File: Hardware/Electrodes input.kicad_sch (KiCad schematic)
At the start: 47 parts, among them J2 Conn_01x26_Pin, U2 TPD4E1B06DRLR

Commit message: DIY_EEG board design changes
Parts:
- removed R1, R10, R11, R12, R13, R14, R15, R16, R2, R3, R4, R5, R6, R7, R8, R9: 220, Resistor_SMD:R_0603_1608Metric, symbol Device:R_US
- removed U2 (x3): TPD4E1B06DRLR, ESD:DRL6_TEX, symbol 2024-02-26_11-45-18:TPD4E1B06DRLR
- added C26: 6.8 uF, Capacitor_SMD:C_0201_0603Metric, symbol Device:C_Small
- added RN1, RN2, RN3, RN4: 4.99 K, Resistor_SMD:R_Array_Convex_4x0402, symbol Device:R_Pack04
- added U3, U4, U5: TPD4E1B06DRLR, tpd4e1b06:DRL6_TEX, symbol 2024-02-26_11-45-18:TPD4E1B06DRLR
- C11, C12, C13, C14, C15, C16, C17, C18, C28, C31, C32, C33, C34, C35, C36, C37, C38, C39: footprint Capacitor_SMD:C_0603_1608Metric_Pad1.08x0.95mm_HandSolder -> Capacitor_SMD:C_0201_0603Metric
- C30: footprint (none) -> Capacitor_SMD:C_0201_0603Metric
- J2: footprint (none) -> Connector_PinHeader_2.54mm:PinHeader_2x13_P2.54mm_Horizontal
- R17: footprint Resistor_SMD:R_0603_1608Metric -> Resistor_SMD:R_0201_0603Metric
- R18, R19, R20, R22: value 220 -> 4.99 K; footprint Resistor_SMD:R_0603_1608Metric -> Resistor_SMD:R_0201_0603Metric
- U2: footprint ESD:DRL6_TEX -> tpd4e1b06:DRL6_TEX
- U6, U9: renamed from U2; footprint ESD:DRL6_TEX -> tpd4e1b06:DRL6_TEX
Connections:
- net AVDD_ED: now also J2.25 (Pin_25), J2.26 (Pin_26); no longer J2.1 (Pin_1), J2.2 (Pin_2)
- net BIAS: now also J2.21 (Pin_21), J2.22 (Pin_22); no longer J2.5 (Pin_5), J2.6 (Pin_6)
- net GNDA: now also C13.1, C17.1, J2.1 (Pin_1), J2.2 (Pin_2), J2.23 (Pin_23), J2.24 (Pin_24), U9.2 (GND), U9.6 (IO4), C26.1, U3.2 (GND), U4.2 (GND), U5.2 (GND); no longer C13.2, C17.2, J2.25 (Pin_25), J2.26 (Pin_26)
- net IN1N: now also C12.2, RN1.2 (R2.1)
- net IN1P: now also C11.2, RN1.1 (R1.1)
- net IN2N: now also C36.2, RN1.4 (R4.1)
- net IN2P: now also C26.2, RN1.3 (R3.1)
- net IN3N: now also C14.2, RN3.2 (R2.1)
- net IN3P: now also C13.2, RN3.1 (R1.1)
- net IN4N: now also C35.2, RN3.4 (R4.1)
- net IN4P: now also C34.2, RN3.3 (R3.1)
- net IN5N: now also C16.2, RN2.2 (R2.1)
- net IN5P: now also C15.2, RN2.1 (R1.1)
- net IN6N: now also C31.2, RN2.4 (R4.1)
- net IN6P: now also C28.2, RN2.3 (R3.1)
- net IN7N: now also C18.2, RN4.2 (R2.1)
- net IN7P: now also C17.2, RN4.1 (R1.1)
- net IN8N: now also C33.2, RN4.4 (R4.1)
- net IN8P: now also C32.2, RN4.3 (R3.1)
- net N1: now also J2.6 (Pin_6), RN1.7 (R2.2); no longer C36.2, J2.21 (Pin_21)
- net N2: now also J2.8 (Pin_8), U2.6 (IO4), RN1.5 (R4.2); no longer C12.2, J2.19 (Pin_19), U2.4 (IO3)
- net N3: now also J2.10 (Pin_10), RN3.7 (R2.2), U3.1 (IO1); no longer C13.1, J2.17 (Pin_17)
- net N4: now also J2.12 (Pin_12), RN3.5 (R4.2), U3.6 (IO4); no longer C35.2, J2.15 (Pin_15)
- net N5: now also J2.14 (Pin_14), RN2.7 (R2.2), U4.1 (IO1); no longer C31.2, J2.13 (Pin_13)
- net N6: now also J2.16 (Pin_16), RN2.5 (R4.2), U4.6 (IO4); no longer C28.2, J2.11 (Pin_11)
- net N7: now also J2.18 (Pin_18), RN4.7 (R2.2), U5.1 (IO1); no longer C17.1, J2.9 (Pin_9)
- net N8: now also J2.20 (Pin_20), RN4.5 (R4.2), U5.6 (IO4); no longer C18.2, J2.7 (Pin_7)
- net P1: now also J2.5 (Pin_5), RN1.8 (R1.2); no longer C11.2, J2.22 (Pin_22)
- net P2: now also J2.7 (Pin_7), U2.4 (IO3), RN1.6 (R3.2); no longer J2.20 (Pin_20), U2.6 (IO4)
- net P3: now also J2.9 (Pin_9), RN3.8 (R1.2), U3.3 (IO2); no longer C34.2, J2.18 (Pin_18)
- net P4: now also J2.11 (Pin_11), RN3.6 (R3.2), U3.4 (IO3); no longer C14.2, J2.16 (Pin_16)
- net P5: now also J2.13 (Pin_13), RN2.8 (R1.2), U4.3 (IO2); no longer C15.2, J2.14 (Pin_14)
- net P6: now also J2.15 (Pin_15), RN2.6 (R3.2), U4.4 (IO3); no longer C16.2, J2.12 (Pin_12)
- net P7: now also J2.17 (Pin_17), RN4.8 (R1.2), U5.3 (IO2); no longer C33.2, J2.10 (Pin_10)
- net P8: now also J2.19 (Pin_19), RN4.6 (R3.2), U5.4 (IO3); no longer C32.2, J2.8 (Pin_8)
- net REF1: now also J2.3 (Pin_3); no longer J2.23 (Pin_23)
- net REF2: now also J2.4 (Pin_4); no longer J2.24 (Pin_24)
- removed net AGND: J2.3 (Pin_3), J2.4 (Pin_4), U9.6 (IO4)
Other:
- moved on the sheet: U2

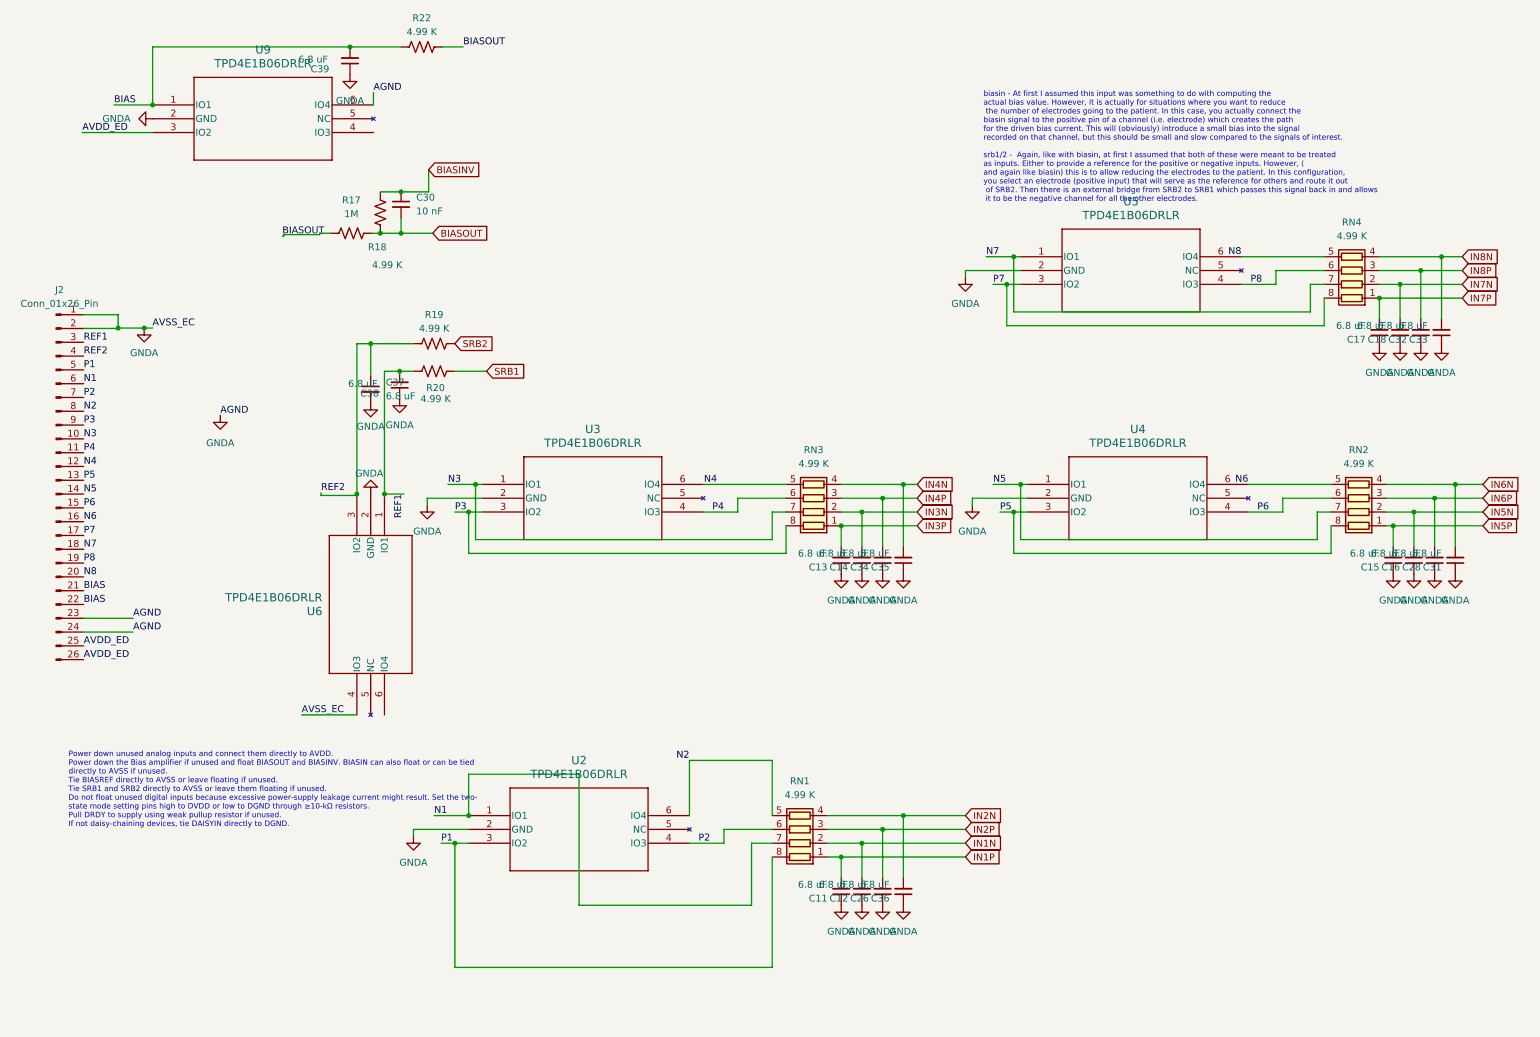
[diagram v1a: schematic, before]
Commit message: redone analog inputs, passive component footprints now match real components, added library for possible 4 element capacitor array
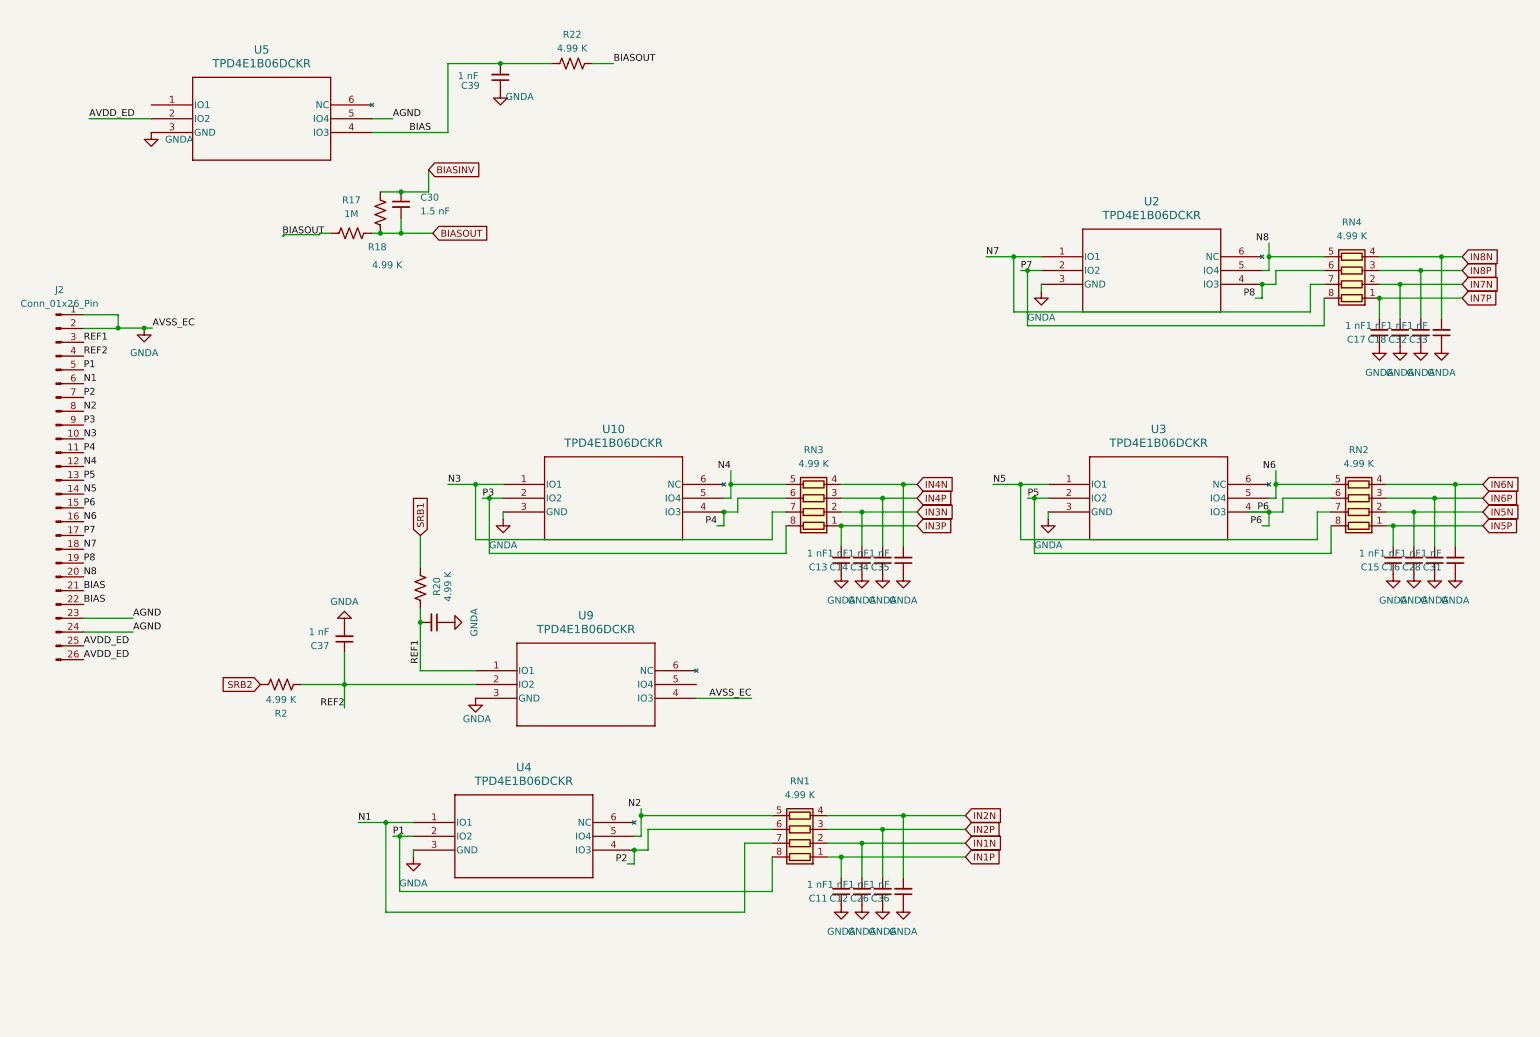
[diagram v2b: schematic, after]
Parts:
- removed R19: 4.99 K, Resistor_SMD:R_0201_0603Metric, symbol Device:R_US
- removed U2, U3, U4, U5, U6, U9: TPD4E1B06DRLR, tpd4e1b06:DRL6_TEX, symbol 2024-02-26_11-45-18:TPD4E1B06DRLR
- added R2: 4.99 K, Resistor_SMD:R_0603_1608Metric, symbol Device:R_US
- added U10, U3, U4, U9: TPD4E1B06DCKR, symbol tpd4e1_esayGND:TPD4E1B06DCKR
- added U2, U5: TPD4E1B06DCKR, TPD4E1B06_R:DCK6_TEX, symbol tpd4e1_esayGND:TPD4E1B06DCKR
- C11, C12, C13, C14, C15, C16, C17, C18, C26, C28, C31, C32, C33, C34, C35, C36, C37, C38, C39: value 6.8 uF -> 1 nF; footprint Capacitor_SMD:C_0201_0603Metric -> Capacitor_SMD:C_0402_1005Metric
- C30: value 10 nF -> 1.5 nF; footprint Capacitor_SMD:C_0201_0603Metric -> Capacitor_SMD:C_0402_1005Metric
- R17, R18, R20, R22: footprint Resistor_SMD:R_0201_0603Metric -> Resistor_SMD:R_0603_1608Metric
- RN4: footprint Resistor_SMD:R_Array_Convex_4x0402 -> Resistor_SMD:R_Array_Convex_4x0603
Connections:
- net AVDD_ED: now also U5.2 (IO2)
- net BIAS: now also U5.4 (IO3)
- net GNDA: now also U10.3 (GND), U2.3 (GND), U3.3 (GND), U4.3 (GND), U5.3 (GND), U9.3 (GND), U9.4 (IO3); no longer J2.23 (Pin_23), J2.24 (Pin_24)
- net N1: now also U4.1 (IO1)
- net N2: now also U4.5 (IO4)
- net N3: now also U10.1 (IO1)
- net N4: now also U10.5 (IO4)
- net N5: now also U3.1 (IO1)
- net N6: now also U3.5 (IO4)
- net N7: now also U2.1 (IO1)
- net N8: now also U2.5 (IO4)
- net P1: now also U4.2 (IO2)
- net P2: now also U4.4 (IO3)
- net P3: now also U10.2 (IO2)
- net P4: now also U10.4 (IO3)
- net P5: now also U3.2 (IO2)
- net P6: now also U3.4 (IO3)
- net P7: now also U2.2 (IO2)
- net P8: now also U2.4 (IO3)
- net REF1: now also U9.1 (IO1)
- net REF2: now also R2.1, U9.2 (IO2)
- net SRB2: now also R2.2
- new net AGND: J2.23 (Pin_23), J2.24 (Pin_24), U5.5 (IO4)
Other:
- note removed: "Power down unused analog inputs and connect them directly to AVDD. Power down the Bias amplifier if unused and float BIASOUT and BIASINV. BIASIN can also float or can be tied directly to AVSS if unused. Tie BIASREF directly to AVSS or leave floating if unused. Tie SRB1 and SRB2 directly to AVSS or leave them floating if unused. Do not float unused digital inputs because excessive power-supply lea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"
- note removed: "biasin - At first I assumed this input was something to do with computing the actual bias value. However, it is actually for situations where you want to reduce the number of electrodes going to the patient. In this case, you actually connect the biasin signal to the positive pin of a channel (i.e. electrode) which creates the path for the driven bias current. This will (obviously) introduce a sm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"
- moved on the sheet: C39, R20, R22

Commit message: redone analog inputs, decoupling caps
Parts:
- RN1, RN2, RN3: footprint Resistor_SMD:R_Array_Convex_4x0402 -> Resistor_SMD:R_Array_Convex_4x0603
- U10, U3, U4, U9: footprint (none) -> TPD4E1B06_R:DCK6_TEX
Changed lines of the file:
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@@
 			)
 		)
-		(property "Footprint" "Resistor_SMD:R_Array_Convex_4x0402"
+		(property "Footprint" "Resistor_SMD:R_Array_Convex_4x0603"
 			(at 153.67 153.035 90)
 			(effects
@@
 			)
 		)
-		(property "Footprint" ""
+		(property "Footprint" "TPD4E1B06_R:DCK6_TEX"
 			(at 93.98 130.81 0)
 			(effects
@@
 			)
 		)
-		(property "Footprint" "Resistor_SMD:R_Array_Convex_4x0402"
+		(property "Footprint" "Resistor_SMD:R_Array_Convex_4x0603"
 			(at 256.54 92.075 90)
 			(effects
@@
 			)
 		)
-		(property "Footprint" ""
+		(property "Footprint" "TPD4E1B06_R:DCK6_TEX"
 			(at 99.06 96.52 0)
 			(effects
@@
 			)
 		)
-		(property "Footprint" ""
+		(property "Footprint" "TPD4E1B06_R:DCK6_TEX"
 			(at 82.55 158.75 0)
 			(effects
@@
 			)
 		)
-		(property "Footprint" "Resistor_SMD:R_Array_Convex_4x0402"
+		(property "Footprint" "Resistor_SMD:R_Array_Convex_4x0603"
 			(at 156.21 92.075 90)
 			(effects
@@
 			)
 		)
-		(property "Footprint" ""
+		(property "Footprint" "TPD4E1B06_R:DCK6_TEX"
 			(at 199.39 96.52 0)
 			(effects

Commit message: Fix Last DRC Errors
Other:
- moved on the sheet: C30

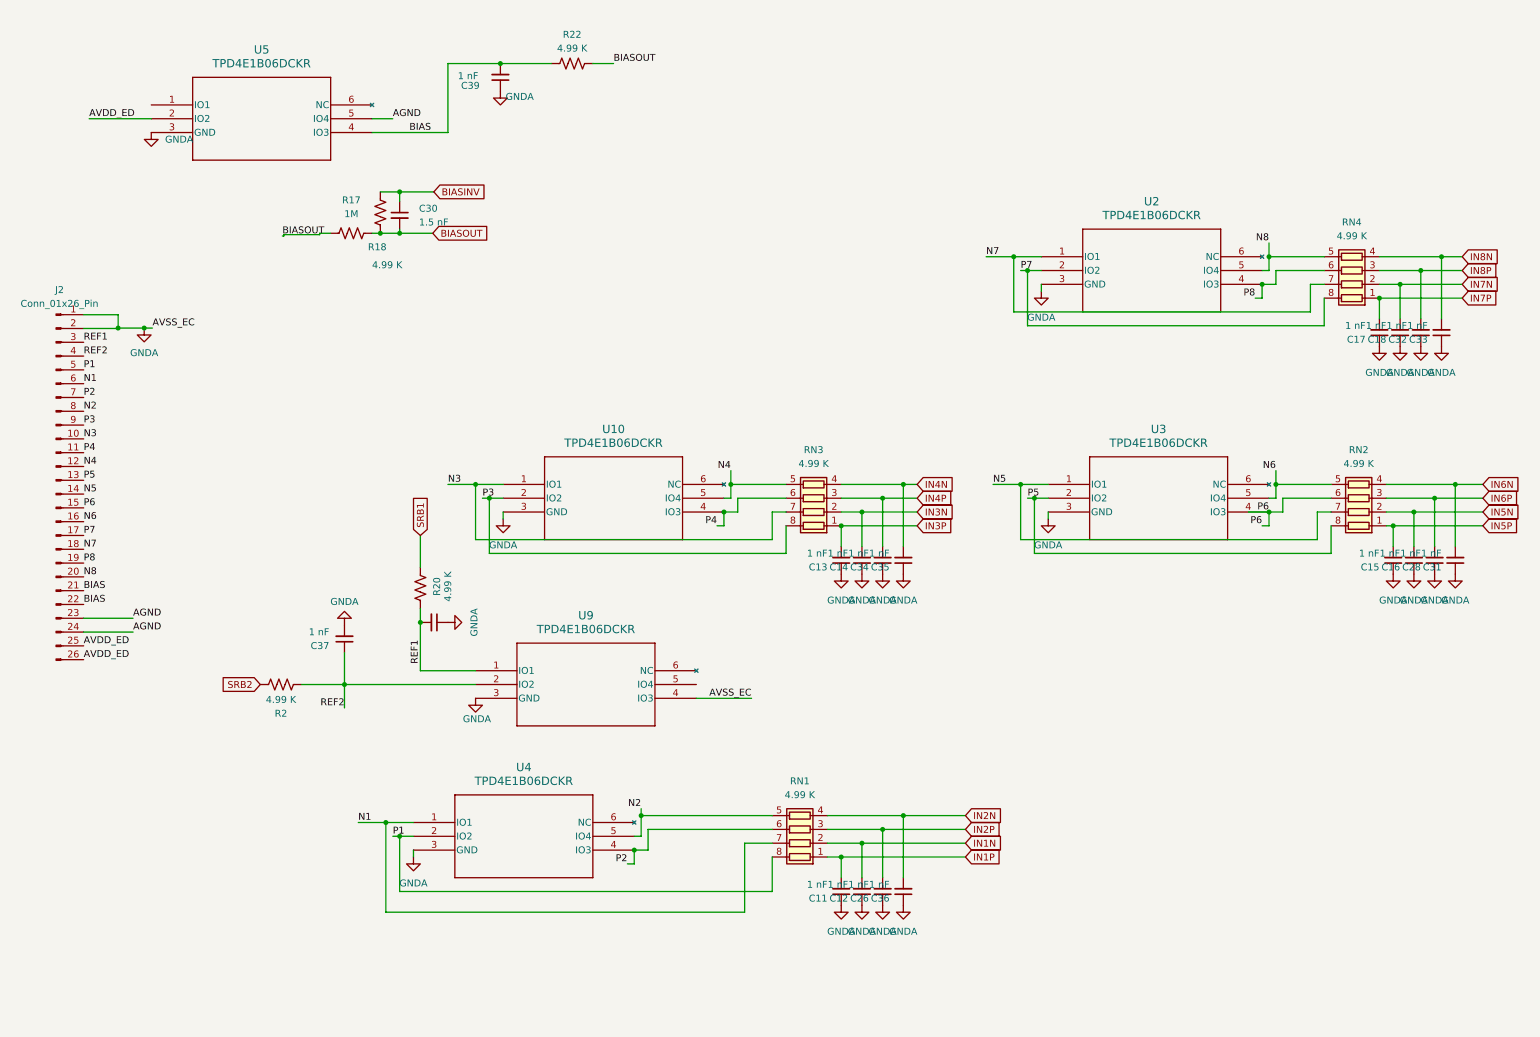
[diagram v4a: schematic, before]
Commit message: Fix Label Error
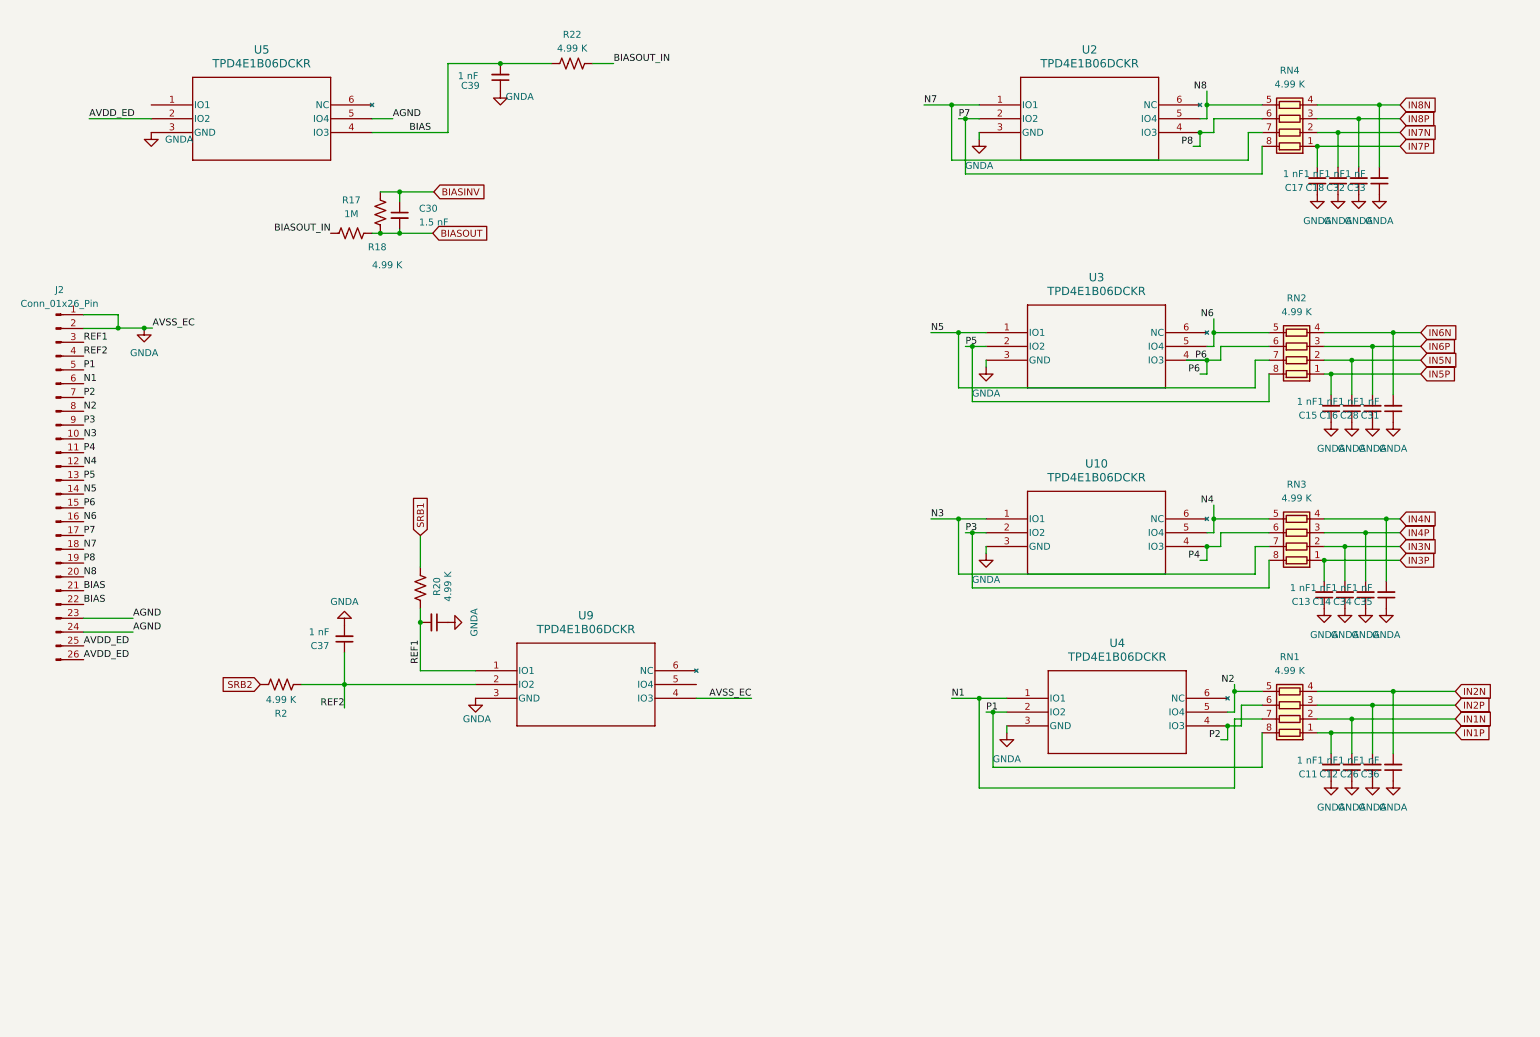
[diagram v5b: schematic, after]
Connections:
- net BIASOUT: no longer R17.1, R22.2
- new net BIASOUT_IN: R17.1, R22.2
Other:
- moved on the sheet: C11, C12, C13, C14, C15, C16, C17, C18, C26, C28, C31, C32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

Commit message: Remove redundant components
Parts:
- R17: value 1M -> 1 MΩ
- R18, R2, R20, R22, RN1, RN2, RN3, RN4: value 4.99 K -> 4.99 KΩ
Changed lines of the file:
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@@
 			)
 		)
-		(property "Value" "4.99 K"
+		(property "Value" "4.99 KΩ"
 			(at 111.76 16.256 90)
 			(effects
@@
 			)
 		)
-		(property "Value" "4.99 K"
+		(property "Value" "4.99 KΩ"
 			(at 243.84 22.86 90)
 			(effects
@@
 			)
 		)
-		(property "Value" "4.99 K"
+		(property "Value" "4.99 KΩ"
 			(at 243.84 130.81 90)
 			(effects
@@
 			)
 		)
-		(property "Value" "4.99 K"
+		(property "Value" "4.99 KΩ"
 			(at 245.11 64.77 90)
 			(effects
@@
 			)
 		)
-		(property "Value" "4.99 K"
+		(property "Value" "4.99 KΩ"
 			(at 74.93 56.134 0)
 			(effects
@@
 			)
 		)
-		(property "Value" "4.99 K"
+		(property "Value" "4.99 KΩ"
 			(at 58.166 136.144 90)
 			(effects
@@
 			)
 		)
-		(property "Value" "4.99 K"
+		(property "Value" "4.99 KΩ"
 			(at 88.9 115.316 90)
 			(effects
@@
 			)
 		)
-		(property "Value" "4.99 K"
+		(property "Value" "4.99 KΩ"
 			(at 245.11 99.06 90)
 			(effects
@@
 			)
 		)
-		(property "Value" "1M"
+		(property "Value" "1 MΩ"
 			(at 71.12 46.736 90)
 			(effects
